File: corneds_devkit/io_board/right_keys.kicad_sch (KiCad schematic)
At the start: 64 parts, among them SW14 SW_Push, SW16 SW_Push, SW18 SW_Push, SW25 SW_Push, SW26 SW_Push, SW27 SW_Push, SW28 SW_Push, SW29 SW_Push, SW30 SW_Push, SW31 SW_Push, SW32 SW_Push, SW33 SW_Push, SW34 SW_Push, SW35 SW_Push, SW36 SW_Push, SW37 SW_Push, SW38 SW_Push, SW39 SW_Push, SW40 SW_Push, SW41 SW_Push, SW42 SW_Push

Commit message: finished mouse and key boards
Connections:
- net rclick_led_di: now reaches D64.1 (DO)
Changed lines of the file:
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@@
+	(wire
+		(pts
+			(xy 135.89 146.05) (xy 138.43 146.05)
+		)
+		(stroke
+			(width 0)
+			(type default)
+		)
+	)
 	(wire
 		(pts
@@
 			(effects
 				(font
+					(size 1.27 1.27)
+				)
+				(justify left)
+				(hide yes)
+			)
+		)
+	)
+	(global_label "rclick_led_di"
+		(shape input)
+		(at 138.43 146.05 0)
+		(fields_autoplaced yes)
+		(effects
+			(font
+				(size 1.27 1.27)
+			)
+			(justify left)
+		)
+		(property "Intersheetrefs" "${INTERSHEET_REFS}"
+			(at 153.2685 146.05 0)
+			(effects
+				(font

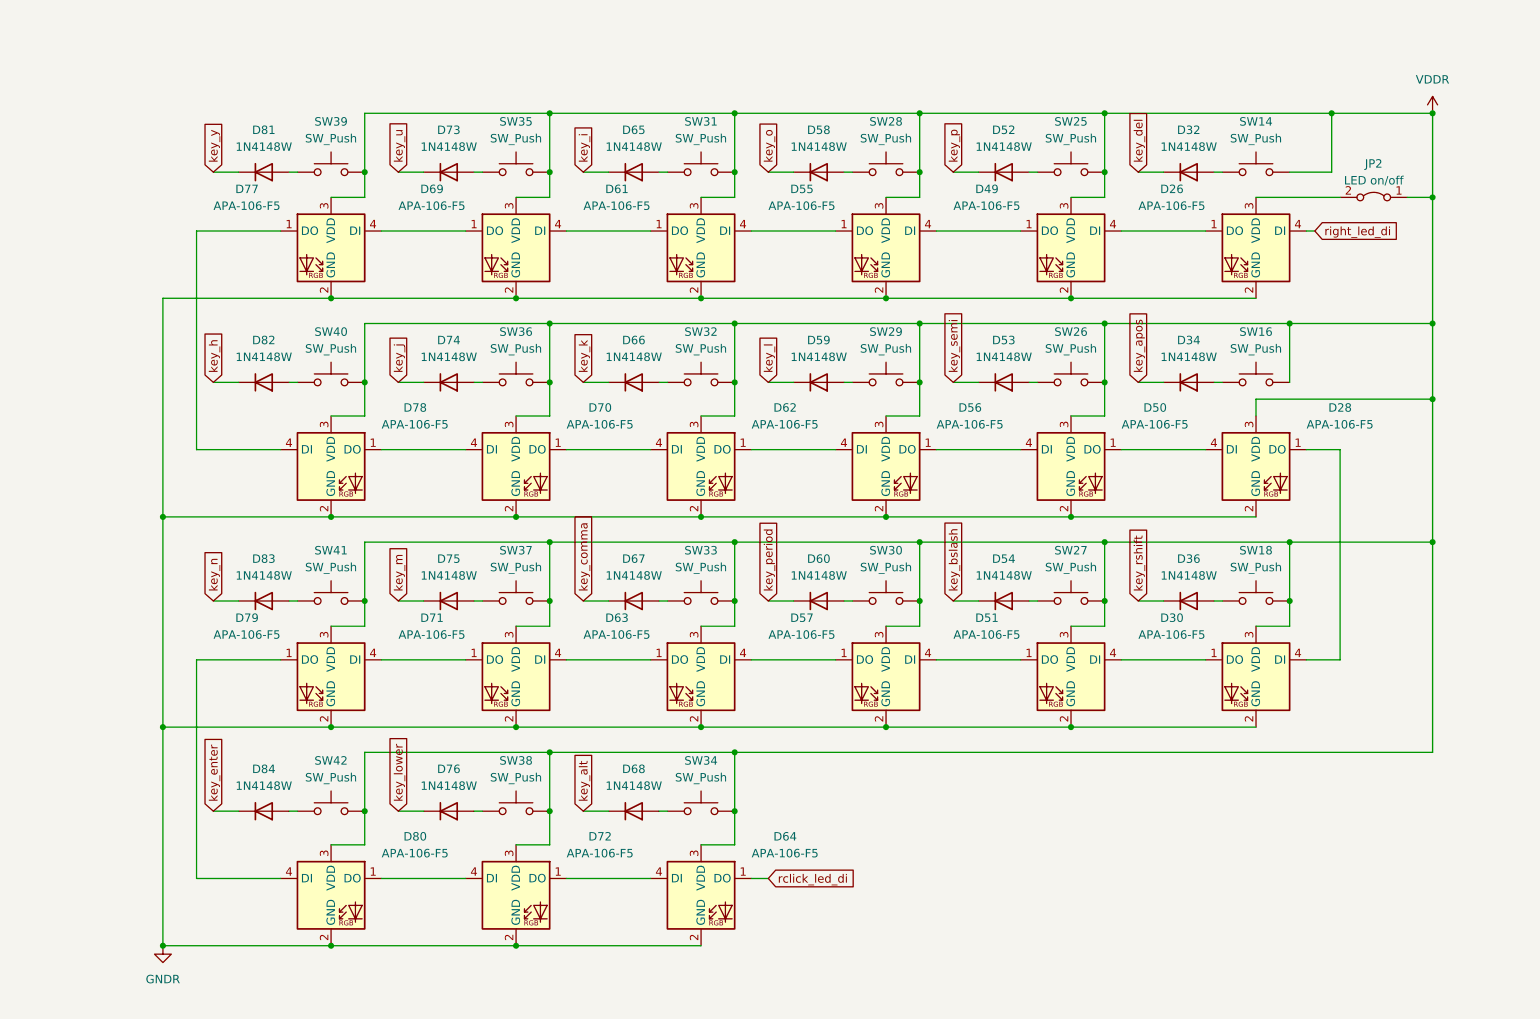
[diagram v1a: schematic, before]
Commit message: finished schematic for io board
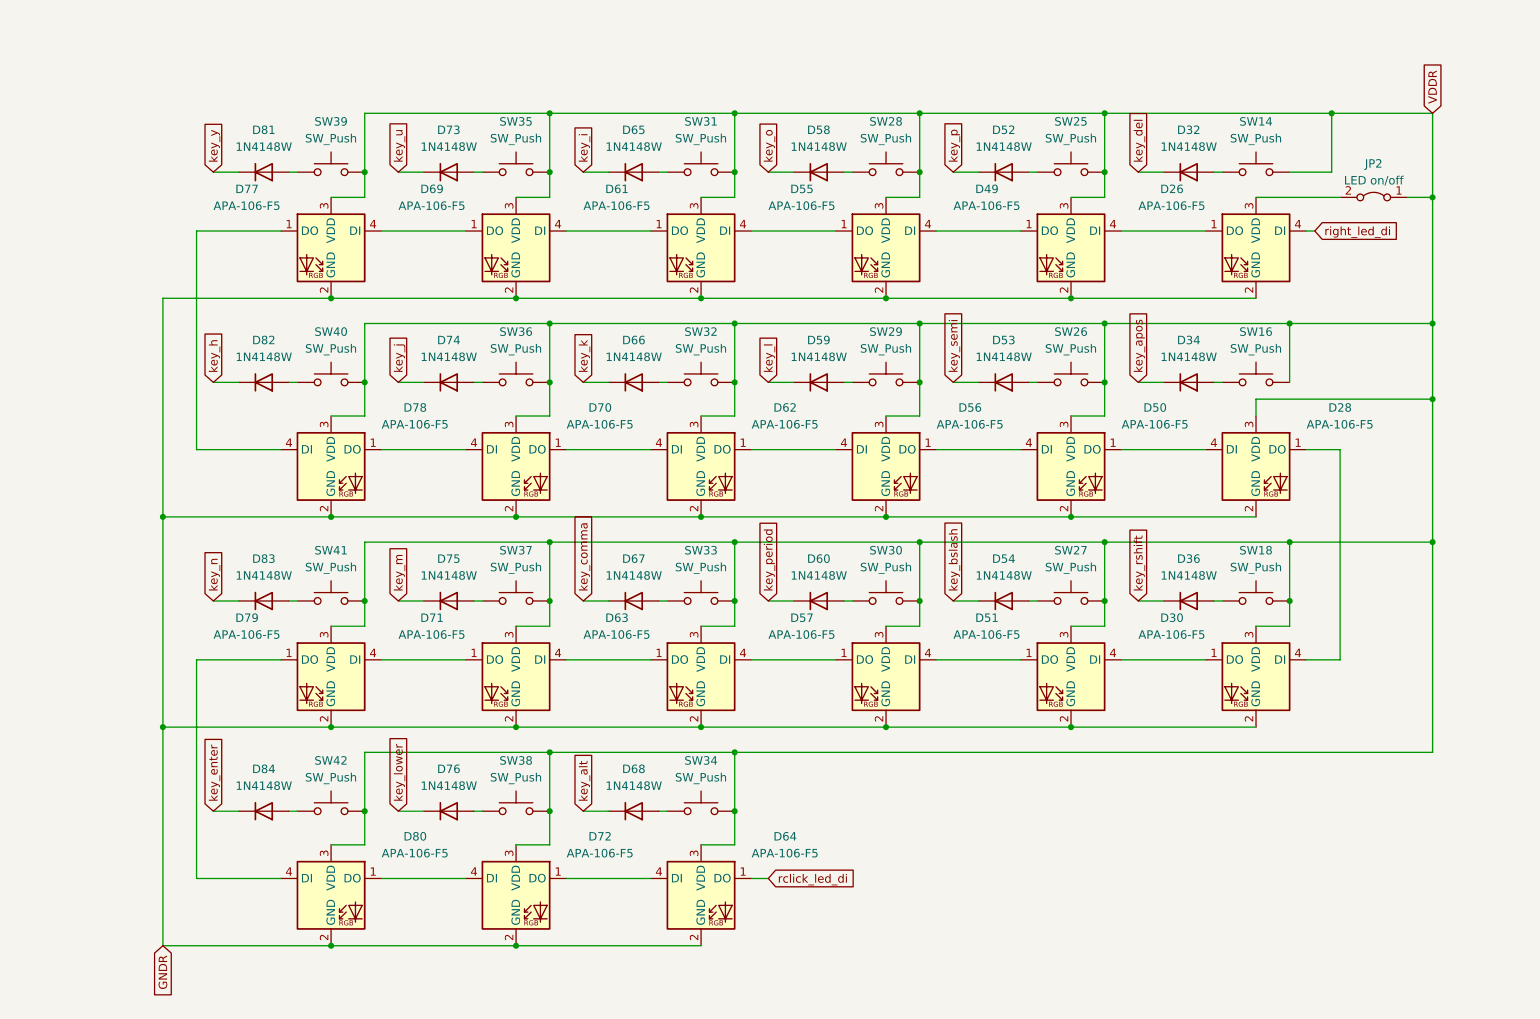
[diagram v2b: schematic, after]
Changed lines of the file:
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@@
 	)
 	(junction
-		(at 46.99 156.21)
-		(diameter 0)
-		(color 0 0 0 0)
-	)
-	(junction
-		(at 238.76 30.48)
-		(diameter 0)
-		(color 0 0 0 0)
-	)
-	(junction
 		(at 156.21 91.44)
 		(diameter 0)
@@
 		)
 	)
+	(global_label "VDDR"
+		(shape input)
+		(at 238.76 30.48 90)
+		(fields_autoplaced yes)
+		(effects
+			(font
+				(size 1.27 1.27)
+			)
+			(justify left)
+		)
+		(property "Intersheetrefs" "${INTERSHEET_REFS}"
+			(at 238.76 22.5962 90)
+			(effects
+				(font
+					(size 1.27 1.27)
+				)
+				(justify left)
+				(hide yes)
+			)
+		)
+	)
 	(global_label "key_comma"
 		(shape input)
@@
 		)
 	)
+	(global_label "GNDR"
+		(shape input)
+		(at 46.99 156.21 270)
+		(fields_autoplaced yes)
+		(effects
+			(font
+				(size 1.27 1.27)
+			)
+			(justify right)
+		)
+		(property "Intersheetrefs" "${INTERSHEET_REFS}"
+			(at 46.99 164.3357 90)
+			(effects
+				(font
+					(size 1.27 1.27)
+				)
+				(justify right)
+				(hide yes)
+			)
+		)
+	)
 	(global_label "key_y"
 		(shape input)
@@
 	)
 	(symbol
-		(lib_id "power:VDD")
-		(at 238.76 30.48 0)
-		(unit 1)
-		(exclude_from_sim no)
-		(in_bom yes)
-		(on_board yes)
-		(dnp no)
-		(fields_autoplaced yes)
-		(property "Reference" "#PWR03"
-			(at 238.76 34.29 0)
-			(effects
-				(font
-					(size 1.27 1.27)
-				)
-				(hide yes)
-			)
-		)
-		(property "Value" "VDDR"
-			(at 238.76 25.4 0)
-			(effects
-				(font
-					(size 1.27 1.27)
-				)
-			)
-		)
-		(property "Footprint" ""
-			(at 238.76 30.48 0)
-			(effects
-				(font
-					(size 1.27 1.27)
-				)
-				(hide yes)
-			)
-		)
-		(property "Datasheet" ""
-			(at 238.76 30.48 0)
-			(effects
-				(font
-					(size 1.27 1.27)
-				)
-				(hide yes)
-			)
-		)
-		(property "Description" "Power symbol creates a global label with name \"VDD\""
-			(at 238.76 30.48 0)
-			(effects
-				(font
-					(size 1.27 1.27)
-				)
-				(hide yes)
-			)
-		)
-		(pin "1"
-		)
-		(instances
-			(project "io_board"
-				(path "/244b6d6b-132d-4d50-ae86-e41103b29008/bd07eb4f-2b61-4923-a58a-bccd1af7bd24"
-					(reference "#PWR03")
-					(unit 1)
-				)
-			)
-		)
-	)
-	(symbol
 		(lib_id "Switch:SW_Push")
 		(at 100.33 39.37 0)
@@
 					(unit 1)
 				)
-			)
-		)
-	)
-	(symbol
-		(lib_id "power:GND1")
-		(at 46.99 156.21 0)
-		(unit 1)
-		(exclude_from_sim no)
-		(in_bom yes)
-		(on_board yes)
-		(dnp no)
-		(fields_autoplaced yes)
-		(property "Reference" "#PWR04"
-			(at 46.99 162.56 0)
-			(effects
-				(font
-					(size 1.27 1.27)
-				)
-				(hide yes)
-			)
-		)
-		(property "Value" "GNDR"
-			(at 46.99 161.29 0)
-			(effects
-				(font
-					(size 1.27 1.27)
-				)
-			)
-		)
-		(property "Footprint" ""
-			(at 46.99 156.21 0)
-			(effects
-				(font
-					(size 1.27 1.27)
-				)
-				(hide yes)
-			)
-		)
-		(property "Datasheet" ""
-			(at 46.99 156.21 0)
-			(effects
-				(font
-					(size 1.27 1.27)
-				)
-				(hide yes)
-			)
-		)
-		(property "Description" "Power symbol creates a global label with name \"GND1\" , ground"
-			(at 46.99 156.21 0)
-			(effects
-				(font
-					(size 1.27 1.27)
-				)
-				(hide yes)
-			)
-		)
-		(pin "1"
-		)
-		(instances
-			(project "io_board"
-				(path "/244b6d6b-132d-4d50-ae86-e41103b29008/bd07eb4f-2b61-4923-a58a-bccd1af7bd24"
-					(reference "#PWR04")
-					(unit 1)
-				)

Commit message: re-routed io board with keypad IC
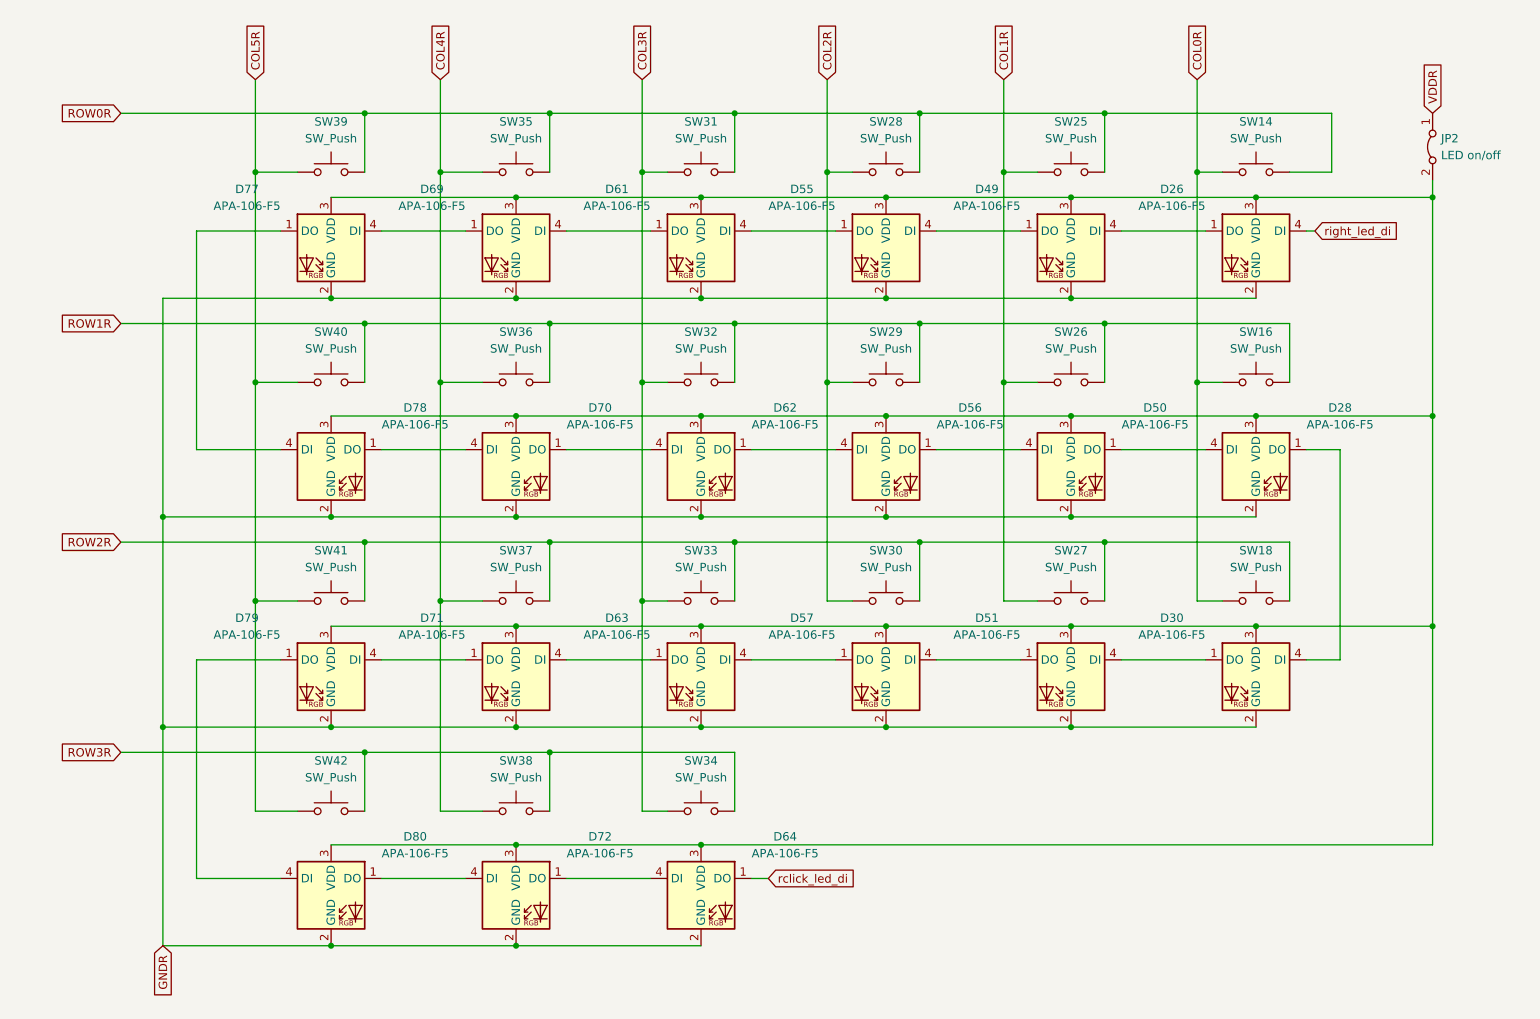
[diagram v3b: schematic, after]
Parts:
- removed D32, D34, D36, D52, D53, D54, D58, D59, D60, D65, D66, D67, D68, D73, D74, D75, D76, D81, D82, D83, D84: 1N4148W, Diode_SMD:D_SOD-123, symbol Diode:1N4148W
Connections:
- net VDDR: no longer D28.3 (VDD), D30.3 (VDD), D49.3 (VDD), D50.3 (VDD), D51.3 (VDD), D55.3 (VDD), D56.3 (VDD), D57.3 (VDD), D61.3 (VDD), D62.3 (VDD), D63.3 (VDD), D64.3 (VDD), D69.3 (VDD), D70.3 (VDD), D71.3 (VDD), D72.3 (VDD), D77.3 (VDD), D78.3 (VDD), D79.3 (VDD), D80.3 (VDD), SW14.1, SW16.1, SW18.1, SW25.1, SW26.1, SW27.1, SW28.1, SW29.1, SW30.1, SW31.1, SW32.1, SW33.1, SW34.1, SW35.1, SW36.1, SW37.1, SW38.1, SW39.1, SW40.1, SW41.1, SW42.1
- net COL2R: now reaches SW30.2
- net COL2R: now also SW28.2, SW29.2
- net COL3R: now reaches SW31.2
- net COL3R: now also SW32.2, SW33.2, SW34.2
- net COL4R: now reaches SW38.2
- net COL4R: now also SW35.2, SW36.2, SW37.2
- net COL5R: now reaches SW39.2
- net COL5R: now also SW40.2, SW41.2, SW42.2
- net COL0R: now reaches SW14.2
- net COL0R: now also SW16.2, SW18.2
- net at D26.3 (VDD), JP2.2 (B): now also D28.3 (VDD), D30.3 (VDD), D49.3 (VDD), D50.3 (VDD), D51.3 (VDD), D55.3 (VDD), D56.3 (VDD), D57.3 (VDD), D61.3 (VDD), D62.3 (VDD), D63.3 (VDD), D64.3 (VDD), D69.3 (VDD), D70.3 (VDD), D71.3 (VDD), D72.3 (VDD), D77.3 (VDD), D78.3 (VDD), D79.3 (VDD), D80.3 (VDD)
- net COL1R: now reaches SW27.2
- net COL1R: now also SW25.2, SW26.2
- new net ROW0R: SW14.1, SW25.1, SW28.1, SW31.1, SW35.1, SW39.1
- new net ROW1R: SW16.1, SW26.1, SW29.1, SW32.1, SW36.1, SW40.1
- new net ROW2R: SW18.1, SW27.1, SW30.1, SW33.1, SW37.1, SW41.1
- new net ROW3R: SW34.1, SW38.1, SW42.1
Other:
- moved on the sheet: JP2

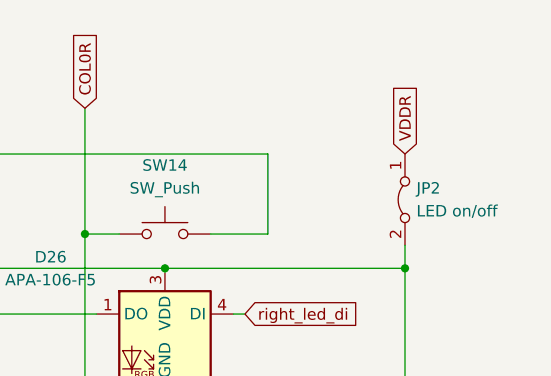
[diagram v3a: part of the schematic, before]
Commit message: added switch footprint, io sch, and keypad IC footprint. Need to find new LEDs and make joystick footprint
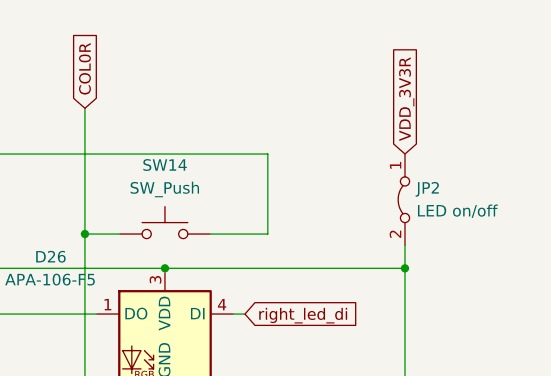
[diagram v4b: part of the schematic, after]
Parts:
- SW14, SW16, SW18, SW25, SW26, SW27, SW28, SW29, SW30, SW31, SW32, SW33, SW34, SW35, SW36, SW37, SW38, SW39, SW40, SW41, SW42: footprint (none) -> key-switches:SW_Gateron_LowProfile_HotSwap_THT
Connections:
- net VDDR renamed VDD_3V3R
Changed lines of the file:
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@@
 		)
 	)
-	(global_label "VDDR"
+	(global_label "VDD_3V3R"
 		(shape input)
 		(at 238.76 30.48 90)
@@
 		)
 		(property "Intersheetrefs" "${INTERSHEET_REFS}"
-			(at 238.76 22.5962 90)
+			(at 238.76 18.121 90)
 			(effects
 				(font
@@
 			)
 		)
-		(property "Footprint" ""
+		(property "Footprint" "key-switches:SW_Gateron_LowProfile_HotSwap_THT"
 			(at 128.27 34.29 0)
 			(effects
@@
 			)
 		)
-		(property "Footprint" ""
+		(property "Footprint" "key-switches:SW_Gateron_LowProfile_HotSwap_THT"
 			(at 100.33 130.81 0)
 			(effects
@@
 			)
 		)
-		(property "Footprint" ""
+		(property "Footprint" "key-switches:SW_Gateron_LowProfile_HotSwap_THT"
 			(at 72.39 34.29 0)
 			(effects
@@
 			)
 		)
-		(property "Footprint" ""
+		(property "Footprint" "key-switches:SW_Gateron_LowProfile_HotSwap_THT"
 			(at 72.39 99.06 0)
 			(effects
@@
 			)
 		)
-		(property "Footprint" ""
+		(property "Footprint" "key-switches:SW_Gateron_LowProfile_HotSwap_THT"
 			(at 156.21 34.29 0)
 			(effects
@@
 			)
 		)
-		(property "Footprint" ""
+		(property "Footprint" "key-switches:SW_Gateron_LowProfile_HotSwap_THT"
 			(at 100.33 66.04 0)
 			(effects
@@
 			)
 		)
-		(property "Footprint" ""
+		(property "Footprint" "key-switches:SW_Gateron_LowProfile_HotSwap_THT"
 			(at 128.27 66.04 0)
 			(effects
@@
 			)
 		)
-		(property "Footprint" ""
+		(property "Footprint" "key-switches:SW_Gateron_LowProfile_HotSwap_THT"
 			(at 100.33 99.06 0)
 			(effects
@@
 			)
 		)
-		(property "Footprint" ""
+		(property "Footprint" "key-switches:SW_Gateron_LowProfile_HotSwap_THT"
 			(at 212.09 34.29 0)
 			(effects
@@
 			)
 		)
-		(property "Footprint" ""
+		(property "Footprint" "key-switches:SW_Gateron_LowProfile_HotSwap_THT"
 			(at 212.09 99.06 0)
 			(effects
@@
 			)
 		)
-		(property "Footprint" ""
+		(property "Footprint" "key-switches:SW_Gateron_LowProfile_HotSwap_THT"
 			(at 184.15 99.06 0)
 			(effects
@@
 			)
 		)
-		(property "Footprint" ""
+		(property "Footprint" "key-switches:SW_Gateron_LowProfile_HotSwap_THT"
 			(at 128.27 99.06 0)
 			(effects
@@
 			)
 		)
-		(property "Footprint" ""
+		(property "Footprint" "key-switches:SW_Gateron_LowProfile_HotSwap_THT"
 			(at 184.15 34.29 0)
 			(effects
@@
 			)
 		)
-		(property "Footprint" ""
+		(property "Footprint" "key-switches:SW_Gateron_LowProfile_HotSwap_THT"
 			(at 212.09 66.04 0)
 			(effects
@@
 			)
 		)
-		(property "Footprint" ""
+		(property "Footprint" "key-switches:SW_Gateron_LowProfile_HotSwap_THT"
 			(at 100.33 34.29 0)
 			(effects
@@
 			)
 		)
-		(property "Footprint" ""
+		(property "Footprint" "key-switches:SW_Gateron_LowProfile_HotSwap_THT"
 			(at 184.15 66.04 0)
 			(effects
@@
 			)
 		)
-		(property "Footprint" ""
+		(property "Footprint" "key-switches:SW_Gateron_LowProfile_HotSwap_THT"
 			(at 128.27 130.81 0)
 			(effects
@@
 			)
 		)
-		(property "Footprint" ""
+		(property "Footprint" "key-switches:SW_Gateron_LowProfile_HotSwap_THT"
 			(at 156.21 99.06 0)
 			(effects
@@
 			)
 		)
-		(property "Footprint" ""
+		(property "Footprint" "key-switches:SW_Gateron_LowProfile_HotSwap_THT"
 			(at 72.39 130.81 0)
 			(effects
@@
 			)
 		)
-		(property "Footprint" ""
+		(property "Footprint" "key-switches:SW_Gateron_LowProfile_HotSwap_THT"
 			(at 72.39 66.04 0)
 			(effects
@@
 			)
 		)
-		(property "Footprint" ""
+		(property "Footprint" "key-switches:SW_Gateron_LowProfile_HotSwap_THT"
 			(at 156.21 66.04 0)
 			(effects

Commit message: io sch done. Need to route
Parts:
- removed JP2: LED on/off, symbol Jumper:Jumper_2_Bridged
- D26, D28, D30, D49, D50, D51, D55, D56, D57, D61, D62, D63, D64, D69, D70, D71, D72, D77, D78, D79, D80: value APA-106-F5 -> SK68XX-SIDE; footprint LED_THT:LED_D5.0mm-4_RGB -> entropy:SK68XX-SIDE
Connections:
- net VDD_5VR: now reaches D26.3 (VDD), D28.3 (VDD), D30.3 (VDD), D49.3 (VDD), D50.3 (VDD), D51.3 (VDD), D55.3 (VDD), D56.3 (VDD), D57.3 (VDD), D61.3 (VDD), D62.3 (VDD), D63.3 (VDD), D64.3 (VDD), D69.3 (VDD), D70.3 (VDD), D71.3 (VDD), D72.3 (VDD), D77.3 (VDD), D78.3 (VDD), D79.3 (VDD), D80.3 (VDD)
